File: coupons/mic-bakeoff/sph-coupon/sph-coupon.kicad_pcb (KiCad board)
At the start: 4 copper layers, 70 x 30 mm, 32 parts, among them J1 Bench 2x05, M1 SPH0641LU4H-1, M2 SPH0641LU4H-1, M3 SPH0641LU4H-1, M4 SPH0641LU4H-1, U1 CDCLVC1112PWR

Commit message: review fixes S10/S11/NIT4: self-consistent coupon quantities, X7R 0603 bypass, ruff pinned
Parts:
- C1, C2, C3, C4, C5, C6, C7, C8: value 100nF C0G -> 100nF X7R
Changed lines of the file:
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@@
 	(fp_text reference "C1" (at 0 -1.2 0) (layer "F.SilkS")
 		(effects (font (size 1.0 1.0) (thickness 0.15)))
-	)	(fp_text value "100nF C0G" (at 0 1.2 0) (layer "F.Fab")
+	)	(fp_text value "100nF X7R" (at 0 1.2 0) (layer "F.Fab")
 		(effects (font (size 1.0 1.0) (thickness 0.15)))
 	)
@@
 	(fp_text reference "C2" (at 0 -1.2 0) (layer "F.SilkS")
 		(effects (font (size 1.0 1.0) (thickness 0.15)))
-	)	(fp_text value "100nF C0G" (at 0 1.2 0) (layer "F.Fab")
+	)	(fp_text value "100nF X7R" (at 0 1.2 0) (layer "F.Fab")
 		(effects (font (size 1.0 1.0) (thickness 0.15)))
 	)
@@
 	(fp_text reference "C3" (at 0 -1.2 0) (layer "F.SilkS")
 		(effects (font (size 1.0 1.0) (thickness 0.15)))
-	)	(fp_text value "100nF C0G" (at 0 1.2 0) (layer "F.Fab")
+	)	(fp_text value "100nF X7R" (at 0 1.2 0) (layer "F.Fab")
 		(effects (font (size 1.0 1.0) (thickness 0.15)))
 	)
@@
 	(fp_text reference "C4" (at 0 -1.2 0) (layer "F.SilkS")
 		(effects (font (size 1.0 1.0) (thickness 0.15)))
-	)	(fp_text value "100nF C0G" (at 0 1.2 0) (layer "F.Fab")
+	)	(fp_text value "100nF X7R" (at 0 1.2 0) (layer "F.Fab")
 		(effects (font (size 1.0 1.0) (thickness 0.15)))
 	)
@@
 	(fp_text reference "C5" (at 0 -1.2 0) (layer "F.SilkS")
 		(effects (font (size 1.0 1.0) (thickness 0.15)))
-	)	(fp_text value "100nF C0G" (at 0 1.2 0) (layer "F.Fab")
+	)	(fp_text value "100nF X7R" (at 0 1.2 0) (layer "F.Fab")
 		(effects (font (size 1.0 1.0) (thickness 0.15)))
 	)
@@
 	(fp_text reference "C6" (at 0 -1.2 0) (layer "F.SilkS")
 		(effects (font (size 1.0 1.0) (thickness 0.15)))
-	)	(fp_text value "100nF C0G" (at 0 1.2 0) (layer "F.Fab")
+	)	(fp_text value "100nF X7R" (at 0 1.2 0) (layer "F.Fab")
 		(effects (font (size 1.0 1.0) (thickness 0.15)))
 	)
@@
 	(fp_text reference "C7" (at 0 -1.2 0) (layer "F.SilkS")
 		(effects (font (size 1.0 1.0) (thickness 0.15)))
-	)	(fp_text value "100nF C0G" (at 0 1.2 0) (layer "F.Fab")
+	)	(fp_text value "100nF X7R" (at 0 1.2 0) (layer "F.Fab")
 		(effects (font (size 1.0 1.0) (thickness 0.15)))
 	)
@@
 	(fp_text reference "C8" (at 0 -1.2 0) (layer "F.SilkS")
 		(effects (font (size 1.0 1.0) (thickness 0.15)))
-	)	(fp_text value "100nF C0G" (at 0 1.2 0) (layer "F.Fab")
-		(effects (font (size 1.0 1.0) (thickness 0.15)))
-	)
+	)	(fp_text value "100nF X7R" (at 0 1.2 0) (layer "F.Fab")
+		(effects (font (size 1.0 1.0) (thickness 0.15)))
+	)

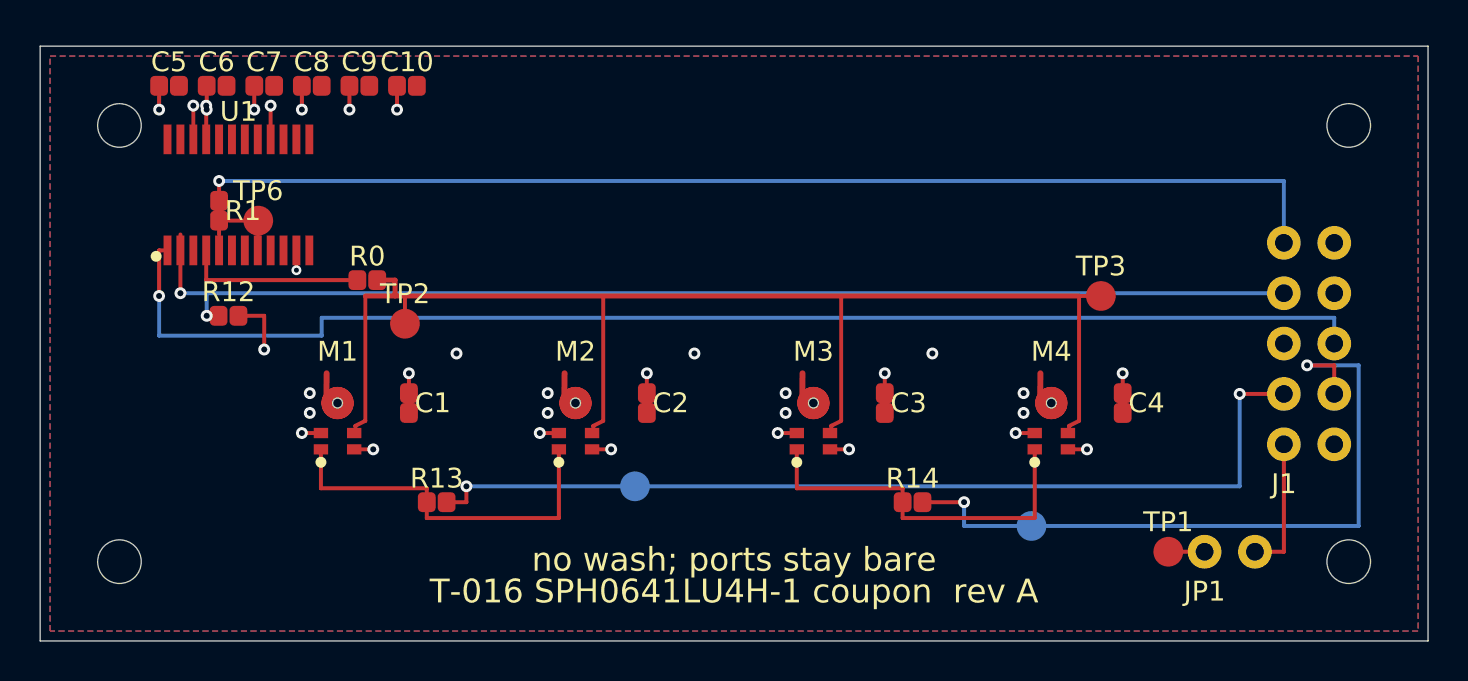
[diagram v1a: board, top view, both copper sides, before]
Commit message: T-022: repair and verify rev B microphone coupons
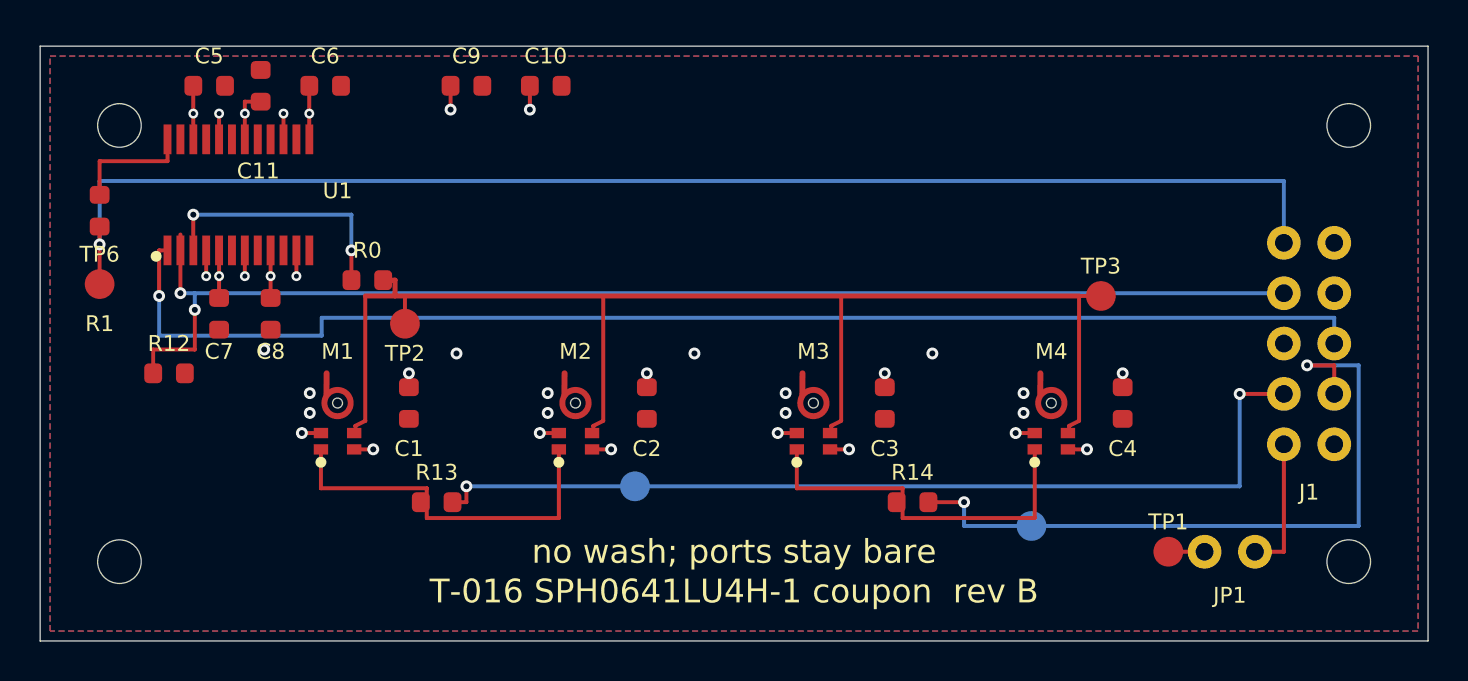
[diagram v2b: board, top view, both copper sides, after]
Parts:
- removed H (x4): M2, coupon:MountingHole_2.2mm_T016
- added C11: 100nF X7R, coupon:C_0603_T016, F.Cu at (11.1, 2.00)
- added H1: M2, coupon:MountingHole_2.2mm_T016, F.Cu at (4.00, 4.00)
- added H2: M2, coupon:MountingHole_2.2mm_T016, F.Cu at (66.0, 4.00)
- added H3: M2, coupon:MountingHole_2.2mm_T016, F.Cu at (4.00, 26.0)
- added H4: M2, coupon:MountingHole_2.2mm_T016, F.Cu at (66.0, 26.0)
- JP1: footprint coupon:PINHEADER_2X01_T016 -> coupon:PINHEADER_1X02_T016
- R0, R1, R12, R13, R14: footprint coupon:C_0603_T016 -> coupon:R_0603_T016
- TP6: value CLK_FBR -> CLK_FB
- moved C7 11.7 mm to (9.03, 13.5), turned to -90 degrees
- moved C8 11.7 mm to (11.6, 13.5), turned to -90 degrees
- moved TP6 8.62 mm to (3.00, 12.0)
- moved C10 7.00 mm to (25.5, 2.00)
- moved R1 6.03 mm to (3.00, 8.30)
- moved C6 5.47 mm to (14.4, 2.00)
- moved C9 5.40 mm to (21.5, 2.00)
- moved R12 4.17 mm to (6.50, 16.5)
- moved C5 2.03 mm to (8.53, 2.00)
- turned TP4 to 180 degrees
- turned TP5 to 180 degrees
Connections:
- R1 pad 1: CLK_FB -> CLK_FBR
- R1 pad 2: CLK_FBR -> CLK_FB
- TP6 pad 1: CLK_FBR -> CLK_FB
- U1 pad 10: GND -> (no net)
- U1 pad 11: +3V3_MIC -> GND
- U1 pad 13: (no net) -> +3V3_MIC
- U1 pad 16: +3V3_MIC -> (no net)
- U1 pad 18: (no net) -> +3V3_MIC
- U1 pad 21: +3V3_MIC -> (no net)
- U1 pad 24: (no net) -> CLK_FBR
- U1 pad 3: GND -> CLK_Y0
- U1 pad 4: CLK_Y0 -> GND
- U1 pad 5: CLK_FBR -> +3V3_MIC
- U1 pad 7: (no net) -> GND
- U1 pad 9: (no net) -> +3V3_MIC
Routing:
- net CLK_FB: track 57.4 -> 69.0 mm
- net +3V3_MIC: track 11.8 -> 22.0 mm, vias 20 -> 17
- net CLK_Y0: track 7.98 -> 13.1 mm, vias 0 -> 2
- net CLK_EN: track 59.8 -> 64.8 mm
- net CLK_FBR: track 1.67 -> 6.22 mm
- net GND: track 8.22 -> 12.1 mm, vias 14 -> 19
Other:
- board text added: "T-016 SPH0641LU4H-1 coupon rev B"
- board text removed: "T-016 SPH0641LU4H-1 coupon rev A"
